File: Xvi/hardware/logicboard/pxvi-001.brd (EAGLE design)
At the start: 100 x 75 mm, 104 parts, among them J1 MKR, J10 THS, J15 TX, J20 GPIO, J21 Grove, J22 Grove, J5 SPI, J7 DIN5, K1 G5V1, P01 TPSTP16R, P02 TPSTP16R, P03 TPSTP16R, P04 TPSTP16R, P05 TPSTP16R, P06 TPSTP16R, P07 TPSTP16SQ, P08 TPSTP16SQ, P09 TPSTP16SQ, P10 TPSTP16SQ, P11 TPSTP16SQ, P12 TPSTP16SQ, Q1 60V/32A/35mΩ, Q10 60V/32A/35mΩ, Q11 60V/32A/35mΩ, Q12 60V/32A/35mΩ, Q13 60V/32A/35mΩ, Q14 60V/32A/35mΩ, Q15 60V/32A/35mΩ, Q16 60V/32A/35mΩ, Q2 60V/32A/35mΩ, Q3 60V/32A/35mΩ, Q4 60V/32A/35mΩ, Q5 60V/32A/35mΩ, Q6 60V/32A/35mΩ, Q7 60V/32A/35mΩ, Q8 60V/32A/35mΩ, Q9 60V/32A/35mΩ, T1 2SC1815, U1 DS18B20, U2 ADAFRUIT-PCA9685, X2 MKDSN1,5/2-5,08

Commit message: RST Sw.
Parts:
- added S1: RST, switch-omron:B3F-31XX
- moved J21 20.0 mm to (70.0, 66.5)
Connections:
- net GND: now also S1.1
- net RST: now also S1.2
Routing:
- net MIRTN: track 62.2 -> 132.0 mm
- net VCC: track 348.4 -> 404.0 mm, vias 0 -> 6
- net RST: track 95.9 -> 151.3 mm
- net GND: track 545.2 -> 498.2 mm, vias 4 -> 8
- net PWM08: track 121.9 -> 75.0 mm, vias 2 -> 5
- net TX: track 107.0 -> 67.1 mm, vias 1 -> 2
- net V+: track 325.0 -> 364.5 mm, vias 16 -> 12
- net LD09: track 83.4 -> 122.7 mm, vias 2 -> 9
- net LD02: track 58.2 -> 95.9 mm, vias 1 -> 7
- net PWM09: track 72.4 -> 100.2 mm
- net LED0: track 51.2 -> 76.2 mm, vias 0 -> 1
- net THS: track 88.0 -> 112.1 mm
- net LD10: track 71.2 -> 47.6 mm
- net LD14: track 44.9 -> 65.4 mm, vias 2 -> 3
- net SCL: track 166.7 -> 147.2 mm
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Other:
- board text added: "Pineapple Xvi 0.1.0-X"
- board text removed: "Pineapple Xvi 0.0.4-X"

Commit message: Fixed Xvi.
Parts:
- removed JP0: RST, pinhead:1X02
- P01, P02: value TPSTP16R -> TPSTP16SQ; device testpad:TP16R -> testpad:TP16SQ
- moved U$1 21.5 mm to (28.0, 16.0), turned to 45 degrees
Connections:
- net GND: no longer JP0.2
- net RST: no longer JP0.1
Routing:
- net PWM08: track 75.0 -> 147.8 mm, vias 5 -> 2
- net MIRTN: track 132.0 -> 60.4 mm, vias 2 -> 1
- net V+: track 364.5 -> 307.8 mm
- net VCC: track 404.0 -> 353.2 mm
- net PWM10: track 86.3 -> 127.9 mm, vias 5 -> 2
- net LD10: track 47.6 -> 86.8 mm, vias 4 -> 2
- net LD09: track 122.7 -> 87.1 mm, vias 9 -> 4
- net PWM09: track 100.2 -> 68.2 mm, vias 3 -> 2
- net LD13: track 47.7 -> 79.0 mm, vias 1 -> 3
- net RST: track 151.3 -> 120.7 mm, vias 3 -> 0
- net LD03: track 68.2 -> 38.8 mm
- net PWM14: track 98.2 -> 73.6 mm, vias 6 -> 3
- net LD14: track 65.4 -> 40.9 mm, vias 3 -> 1
- net LD01: track 58.9 -> 82.6 mm, vias 1 -> 7
- net PWM05: track 78.6 -> 55.2 mm, vias 0 -> 1
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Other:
- board text added: "FAN 30mm x 30mm"
- board text added: "Pineapple Xvi 0.1.1-X"
- board text removed: "Pineapple Xvi 0.1.0-X"

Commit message: Fixed bugs.
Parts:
- removed C101, C102, C103, C104, C105, C106, C107, C108, C109, C110, C111, C112, C113, C114, C115, C116: 10u, rcl:C3216
- removed P01, P02, P07, P08, P09, P10, P11, P12: TPSTP16SQ, testpad:TP16SQ
- removed P03, P04, P05, P06: TPSTP16R, testpad:TP16R
- removed X2: MKDSN1,5/2-5,08, con-phoenix-508:MKDSN1,5/2-5,08
- added JP1: (no value), pinhead:1X02
- C1: value 22u -> 10u; device rcl:C025-050X050 -> rcl:C025-024X044
- C2: value 470n -> 100n; device rcl:C050-024X044 -> rcl:C025-030X050
- C3: value 1u -> 47u; device rcl:C050-024X044 -> rcl:C025-050X050
- C4: device rcl:C025-024X044 -> rcl:C025-030X050
- V1: device v-reg:78XXL -> v-reg:78XXS
- moved U1 35.3 mm to (58.0, 20.0), turned to 90 degrees
- moved D3 14.0 mm to (43.0, 20.0)
- moved R6 7.62 mm to (40.0, 13.0)
- moved C1 4.50 mm to (94.0, 17.5)
- moved D2 3.50 mm to (6.50, 37.5)
- moved C2 3.00 mm to (94.0, 20.5)
- moved D1 3.00 mm to (94.0, 49.5)
- moved F1 2.50 mm to (94.0, 46.0)
- moved V1 2.50 mm to (94.0, 28.0)
- moved C3 2.00 mm to (94.0, 53.0)
- moved R2 1.50 mm to (8.50, 54.5)
- moved R5 1.50 mm to (85.5, 56.5)
- moved C7 1.00 mm to (34.5, 3.50)
- moved R4 1.00 mm to (85.5, 58.5)
- moved C100 0.50 mm to (40.0, 3.50)
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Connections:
- net ANLG0: no longer P03.TP
- net ANLG1: no longer P04.TP
- net ANLG2: no longer P05.TP
- net ANLG3: no longer P06.TP
- net DTCT0: no longer P09.TP
- net DTCT1: no longer P10.TP
- net DTCT2: no longer P11.TP
- net DTCT3: no longer P12.TP
- net FAN: now also JP1.1; no longer X2.2
- net GND: now also JP1.2; no longer P01.TP, P07.TP, X2.1
- net LD00: no longer C101.2
- net LD01: no longer C102.2
- net LD02: no longer C103.2
- net LD03: no longer C104.2
- net LD04: no longer C105.2
- net LD05: no longer C106.2
- net LD06: no longer C107.2
- net LD07: no longer C108.2
- net LD08: no longer C109.2
- net LD09: no longer C110.2
- net LD10: no longer C111.2
- net LD11: no longer C112.2
- net LD12: no longer C113.2
- net LD13: no longer C114.2
- net LD14: no longer C115.2
- net LD15: no longer C116.2
- net V+: no longer C101.1, C102.1, C103.1, C104.1, C105.1, C106.1, C107.1, C108.1, C109.1, C110.1, C111.1, C112.1, C113.1, C114.1, C115.1, C116.1
- net VCC: no longer P02.TP, P08.TP
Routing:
- net PWM08: track 147.8 -> 79.9 mm
- net V+: track 307.8 -> 240.0 mm, vias 12 -> 4
- net LD02: track 99.4 -> 48.7 mm, vias 1 -> 0
- net GND: track 512.8 -> 473.0 mm, vias 7 -> 4
- net DTCT1: track 38.6 -> 0.00 mm
- net DTCT0: track 38.4 -> 0.00 mm
- net GPIO1: track 96.7 -> 60.3 mm
- net DTCT3: track 33.5 -> 0.00 mm, vias 2 -> 0
- net DTCT2: track 33.4 -> 0.00 mm
- net MISND: track 54.3 -> 87.0 mm
- net LD01: track 82.6 -> 51.8 mm, vias 7 -> 1
- net LD10: track 86.8 -> 56.6 mm
- net LD00: track 85.9 -> 57.9 mm, vias 2 -> 3
- net VCC: track 353.2 -> 380.9 mm, vias 6 -> 2
- net SCL: track 143.9 -> 171.4 mm, vias 4 -> 3
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- removed copper zone on layer 1, net GND
- removed copper zone on layer 16, net GND
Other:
- board text removed: "A0"
- board text removed: "A1"
- board text removed: "A2"
- board text removed: "A3"
- board text removed: "X0"
- board text removed: "X1"
- board text removed: "X2"
- board text removed: "X3"

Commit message: MIDI Phantom.
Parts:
- added S2: MIDIPHANTOM, switch-dil:DIP02YL
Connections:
- new net MIDIINGND: J7.1, S2.1
- new net MIDIINV+: J7.3, S2.2
- net GND: now also S2.4
- net V+: now also S2.3
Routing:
- net MIDIINGND: track 0.00 -> 57.3 mm, vias 0 -> 1
- net PWM09: track 78.9 -> 134.2 mm, vias 2 -> 1
- net PWM10: track 113.2 -> 76.2 mm
- net MIDIINV+: track 0.00 -> 36.9 mm, vias 0 -> 2
- net GND: track 473.0 -> 500.4 mm, vias 4 -> 6
- net LD11: track 87.5 -> 62.0 mm
- net MISND: track 87.0 -> 62.4 mm, vias 2 -> 1
- net PWM07: track 58.6 -> 80.8 mm, vias 1 -> 0
- net PWM11: track 78.3 -> 99.1 mm, vias 2 -> 0
- net LD00: track 57.9 -> 78.5 mm, vias 3 -> 1
- net LD13: track 59.4 -> 40.5 mm, vias 1 -> 3
- net LD12: track 57.3 -> 40.5 mm, vias 0 -> 6
- net LD10: track 56.6 -> 73.3 mm, vias 2 -> 1
- net D7GATE: track 107.7 -> 93.0 mm
- net SCL: track 171.4 -> 157.3 mm, vias 3 -> 6
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- added copper zone on layer 1, net GND
- added copper zone on layer 16, net GND
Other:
- board text added: "MIDI PHANTOM"
- board text removed: "7805"

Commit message: Fixed some errors.
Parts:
- JP1: value (none) -> Fan
- R2: value 10k -> 47k
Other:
- board text added: "Fan"
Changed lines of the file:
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@@
 <wire x1="50" y1="17" x2="71" y2="37.5" width="0.15" layer="22" style="longdash"/>
 <wire x1="71" y1="37.5" x2="50" y2="59" width="0.15" layer="22" style="longdash"/>
+<text x="3" y="42" size="1" layer="25" rot="R90" align="center">Fan</text>
 </plain>
 <attributes>
@@
 <attribute name="VALUE" x="8.8114" y="52.3664" size="0.9906" layer="27" ratio="10" rot="R90"/>
 </element>
-<element name="R2" library="resistor" library_urn="urn:adsk.eagle:library:348" package="0204/5" package3d_urn="urn:adsk.eagle:package:23488/1" value="10k" x="8.5" y="54.5" smashed="yes" rot="R90">
+<element name="R2" library="resistor" library_urn="urn:adsk.eagle:library:348" package="0204/5" package3d_urn="urn:adsk.eagle:package:23488/1" value="47k" x="8.5" y="54.5" smashed="yes" rot="R90">
 <attribute name="NAME" x="8.5" y="58.5" size="1" layer="25" ratio="10" align="center"/>
 <attribute name="VALUE" x="10.8114" y="52.3664" size="0.9906" layer="27" ratio="10" rot="R90"/>
@@
 <attribute name="VALUE" x="46.317" y="75.969" size="1.27" layer="28" ratio="10" rot="MR180"/>
 </element>
-<element name="JP1" library="pinhead" library_urn="urn:adsk.eagle:library:325" package="1X02" package3d_urn="urn:adsk.eagle:package:22435/2" value="" x="3" y="37.5" smashed="yes" rot="R270">
+<element name="JP1" library="pinhead" library_urn="urn:adsk.eagle:library:325" package="1X02" package3d_urn="urn:adsk.eagle:package:22435/2" value="Fan" x="3" y="37.5" smashed="yes" rot="R270">
 <attribute name="NAME" x="0.5" y="37.5" size="1" layer="25" ratio="10" rot="R90" align="center"/>
 <attribute name="POPULARITY" value="98" x="3" y="37.5" size="1.778" layer="27" rot="R270" display="off"/>

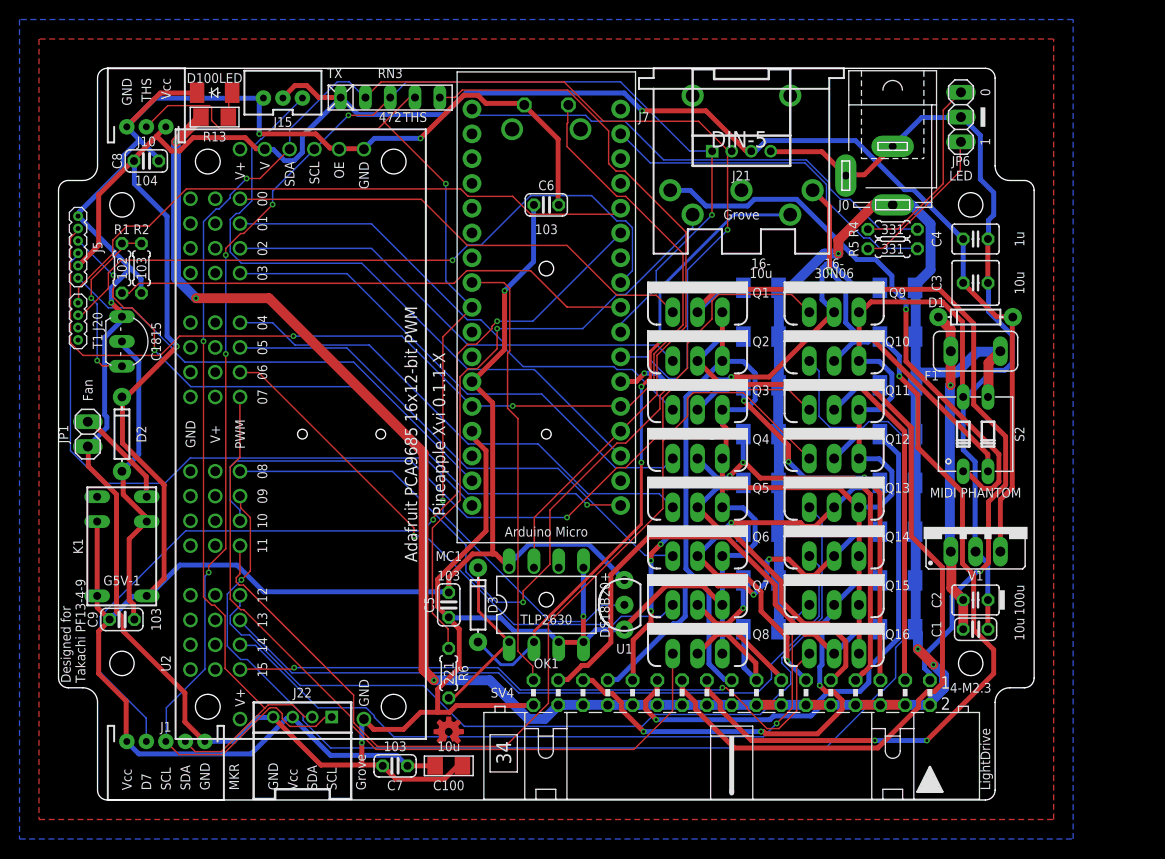
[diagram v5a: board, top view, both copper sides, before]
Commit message: Added 5V-direct-injection mode.
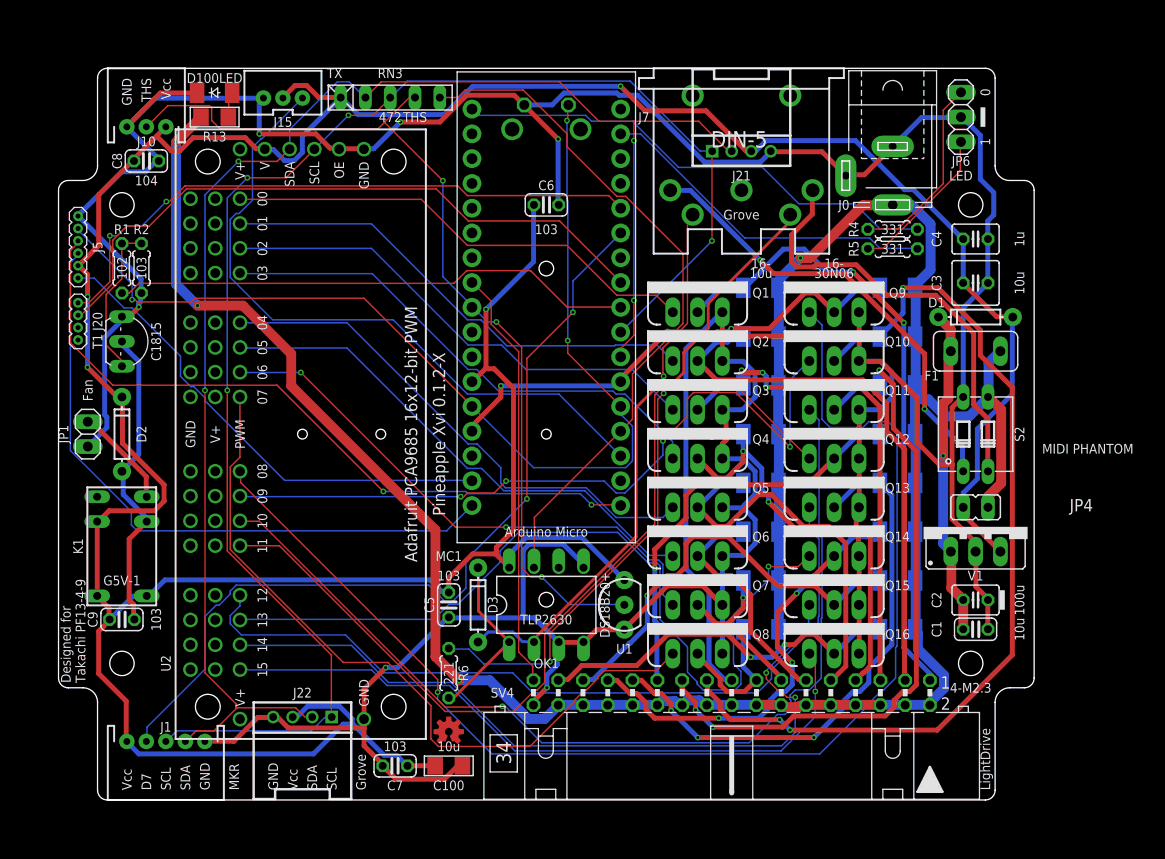
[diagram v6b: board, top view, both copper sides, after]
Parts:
- added JP4: (no value), jumper:JP1
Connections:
- net V+: now also JP4.1
- net VCC: now also JP4.2
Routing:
- net PWM09: track 134.2 -> 75.7 mm, vias 1 -> 4
- net PWM08: track 86.6 -> 130.0 mm
- net PWM10: track 76.2 -> 100.8 mm
- net GND: track 500.4 -> 478.3 mm, vias 6 -> 8
- net LD11: track 62.0 -> 42.9 mm
- net LD12: track 40.5 -> 57.5 mm, vias 6 -> 3
- net LD00: track 78.5 -> 64.7 mm, vias 1 -> 2
- net LD09: track 80.9 -> 93.7 mm
- net PWM13: track 73.3 -> 86.0 mm, vias 0 -> 1
- net LD15: track 50.3 -> 38.7 mm, vias 0 -> 2
- net MIDIINGND: track 57.3 -> 46.7 mm, vias 1 -> 2
- net SDA: track 166.9 -> 157.7 mm, vias 3 -> 4
- net V+: track 250.0 -> 259.1 mm, vias 6 -> 4
- net MIDIINV+: track 36.9 -> 44.9 mm, vias 2 -> 0
- net LD04: track 32.5 -> 39.9 mm
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- removed copper zone on layer 1, net GND
- removed copper zone on layer 16, net GND
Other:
- board text added: "Pineapple Xvi 0.1.2-X"
- board text removed: "Pineapple Xvi 0.1.1-X"

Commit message: 5V direct injection pins.
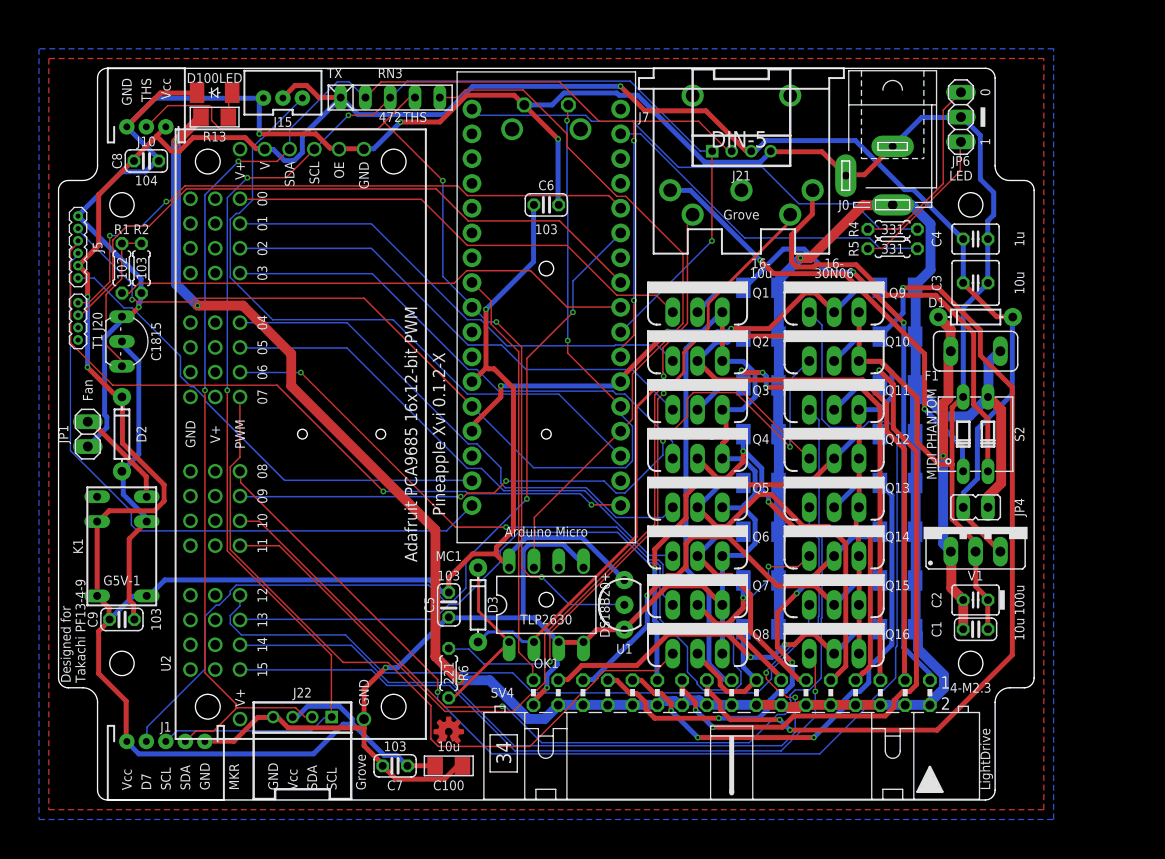
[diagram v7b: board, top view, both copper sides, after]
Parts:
- JP4: value (none) -> 5V Dircet
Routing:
- added copper zone on layer 1, net GND
- added copper zone on layer 16, net GND
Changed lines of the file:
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@@
 <setting verticaltext="up"/>
 </settings>
-<grid distance="0.5" unitdist="mm" unit="mm" style="lines" multiple="2" display="yes" altdistance="50" altunitdist="mil" altunit="mil"/>
+<grid distance="1" unitdist="mm" unit="mm" style="lines" multiple="2" display="yes" altdistance="50" altunitdist="mil" altunit="mil"/>
 <layers>
 <layer number="1" name="Top" color="4" fill="1" visible="yes" active="yes"/>
@@
 <text x="10" y="47" size="1" layer="25" rot="R90" align="center">C1815</text>
 <text x="79.5" y="54" size="1" layer="25" align="center">30N06</text>
-<text x="105.5" y="36" size="1" layer="25" align="center">MIDI PHANTOM</text>
+<text x="89.5" y="37.5" size="1" layer="25" rot="R90" align="center">MIDI PHANTOM</text>
 <text x="11" y="1" size="1" layer="26" rot="MR90" align="center-left">SCL</text>
 <text x="7" y="1" size="1" layer="26" rot="MR90" align="center-left">Vcc</text>
@@
 <attribute name="VALUE" x="97.5052" y="34.3504" size="1.27" layer="27" ratio="10" rot="R90"/>
 </element>
-<element name="JP4" library="jumper" library_urn="urn:adsk.eagle:library:252" package="JP1" package3d_urn="urn:adsk.eagle:package:15455/1" value="" x="94" y="30" smashed="yes" rot="R90">
-<attribute name="NAME" x="106.04" y="30.849" size="1.27" layer="25" ratio="10" rot="R180"/>
+<element name="JP4" library="jumper" library_urn="urn:adsk.eagle:library:252" package="JP1" package3d_urn="urn:adsk.eagle:package:15455/1" value="5V Dircet" x="94" y="30" smashed="yes" rot="R90">
+<attribute name="NAME" x="98.5" y="30" size="1" layer="25" ratio="10" rot="R90" align="center"/>
 <attribute name="POPULARITY" value="61" x="94" y="30" size="1.778" layer="27" rot="R90" display="off"/>
 <attribute name="VALUE" x="96.54" y="32.921" size="1.27" layer="27" ratio="10" rot="R180"/>
@@
 <via x="51.2064" y="67.7418" extent="1-16" drill="0.3048"/>
 <via x="35.052" y="69.4944" extent="1-16" drill="0.3048"/>
+<polygon width="0.2" layer="1">
+<vertex x="-1" y="-1"/>
+<vertex x="101" y="-1"/>
+<vertex x="101" y="76"/>
+<vertex x="-1" y="76"/>
+</polygon>
+<polygon width="0.2" layer="16">
+<vertex x="-2" y="-2"/>
+<vertex x="102" y="-2"/>
+<vertex x="102" y="77"/>
+<vertex x="-2" y="77"/>
+</polygon>
 </signal>
 <signal name="VCC" class="2">
